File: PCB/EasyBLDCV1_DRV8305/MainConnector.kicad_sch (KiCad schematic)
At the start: 20 parts, among them J1 10159560-A00221RLF, U4 LMR16006XDDCR

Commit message: Colored main connector
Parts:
- L1: footprint EasyBLDC:SD53 -> Inductor_SMD:L_Changjiang_FNR4020S
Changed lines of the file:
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@@
 			)
 		)
-		(property "Footprint" "EasyBLDC:SD53"
+		(property "Footprint" "Inductor_SMD:L_Changjiang_FNR4020S"
 			(at 204.47 45.72 0)
 			(effects

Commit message: Fixed errors with silkscreen overlaping vias. Generated final gerbers.
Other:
- company: Buckley Boards  -> Peter Buckley Engineering
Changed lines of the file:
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@@
 		(date "2024-08-06")
 		(rev "1.0")
-		(company "Buckley Boards ")
+		(company "Peter Buckley Engineering")
 	)
 	(junction

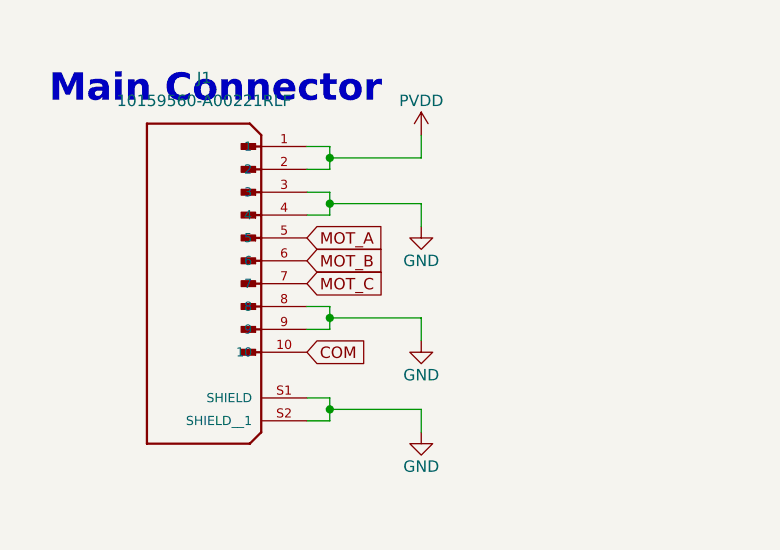
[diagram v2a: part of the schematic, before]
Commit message: Changed main connector pinout to improve signal integrity
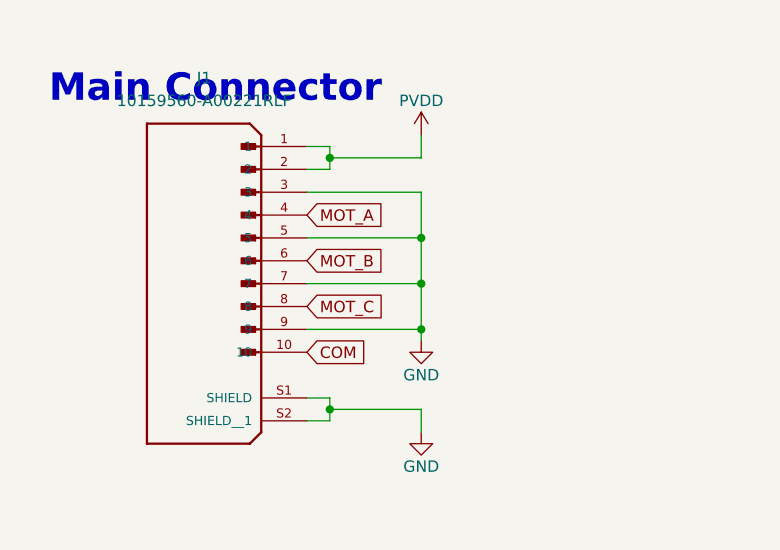
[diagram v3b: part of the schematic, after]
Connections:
- net GND: now also J1.5, J1.7; no longer J1.4, J1.8
- net MOT_A: now also J1.4; no longer J1.5
- net MOT_C: now also J1.8; no longer J1.7
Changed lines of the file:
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@@
-	)
-	(junction
-		(at 78.74 67.31)
-		(diameter 0)
-		(color 0 0 0 0)
 	)
 	(junction
@@
 	)
 	(junction
+		(at 88.9 58.42)
+		(diameter 0)
+		(color 0 0 0 0)
+	)
+	(junction
+		(at 88.9 68.58)
+		(diameter 0)
+		(color 0 0 0 0)
+	)
+	(junction
 		(at 195.58 45.72)
+		(diameter 0)
+		(color 0 0 0 0)
+	)
+	(junction
+		(at 88.9 63.5)
 		(diameter 0)
 		(color 0 0 0 0)
@@
 	)
 	(junction
-		(at 78.74 54.61)
-		(diameter 0)
-		(color 0 0 0 0)
-	)
-	(junction
 		(at 73.66 116.84)
 		(diameter 0)
@@
 	(wire
 		(pts
-			(xy 78.74 68.58) (xy 76.2 68.58)
+			(xy 76.2 68.58) (xy 88.9 68.58)
 		)
 		(stroke
@@
 	(wire
 		(pts
-			(xy 78.74 54.61) (xy 88.9 54.61)
-		)
-		(stroke
-			(width 0)
-			(type default)
-		)
-	)
-	(wire
-		(pts
 			(xy 210.82 76.2) (xy 210.82 78.74)
 		)
@@
 	(wire
 		(pts
+			(xy 88.9 58.42) (xy 88.9 63.5)
+		)
+		(stroke
+			(width 0)
+			(type default)
+		)
+	)
+	(wire
+		(pts
+			(xy 76.2 58.42) (xy 88.9 58.42)
+		)
+		(stroke
+			(width 0)
+			(type default)
+		)
+	)
+	(wire
+		(pts
 			(xy 49.53 114.3) (xy 49.53 116.84)
 		)
@@
 	(wire
 		(pts
-			(xy 76.2 55.88) (xy 78.74 55.88)
-		)
-		(stroke
-			(width 0)
-			(type default)
-		)
-	)
-	(wire
-		(pts
 			(xy 201.93 60.96) (xy 201.93 64.77)
 		)
@@
 	(wire
 		(pts
-			(xy 76.2 66.04) (xy 78.74 66.04)
-		)
-		(stroke
-			(width 0)
-			(type default)
-		)
-	)
-	(wire
-		(pts
 			(xy 182.88 78.74) (xy 210.82 78.74)
 		)
@@
 	(wire
 		(pts
-			(xy 78.74 54.61) (xy 78.74 53.34)
-		)
-		(stroke
-			(width 0)
-			(type default)
-		)
-	)
-	(wire
-		(pts
 			(xy 86.36 135.89) (xy 86.36 137.16)
 		)
@@
 	(wire
 		(pts
-			(xy 78.74 67.31) (xy 88.9 67.31)
-		)
-		(stroke
-			(width 0)
-			(type default)
-		)
-	)
-	(wire
-		(pts
-			(xy 78.74 53.34) (xy 76.2 53.34)
+			(xy 88.9 63.5) (xy 88.9 68.58)
+		)
+		(stroke
+			(width 0)
+			(type default)
+		)
+	)
+	(wire
+		(pts
+			(xy 88.9 53.34) (xy 88.9 58.42)
 		)
 		(stroke
@@
 	(wire
 		(pts
-			(xy 78.74 55.88) (xy 78.74 54.61)
-		)
-		(stroke
-			(width 0)
-			(type default)
-		)
-	)
-	(wire
-		(pts
-			(xy 78.74 66.04) (xy 78.74 67.31)
-		)
-		(stroke
-			(width 0)
-			(type default)
-		)
-	)
-	(wire
-		(pts
 			(xy 78.74 49.53) (xy 88.9 49.53)
 		)
@@
 	(wire
 		(pts
-			(xy 88.9 67.31) (xy 88.9 69.85)
+			(xy 88.9 68.58) (xy 88.9 69.85)
+		)
+		(stroke
+			(width 0)
+			(type default)
+		)
+	)
+	(wire
+		(pts
+			(xy 76.2 63.5) (xy 88.9 63.5)
 		)
 		(stroke
@@
 	(wire
 		(pts
-			(xy 88.9 54.61) (xy 88.9 57.15)
-		)
-		(stroke
-			(width 0)
-			(type default)
-		)
-	)
-	(wire
-		(pts
 			(xy 73.66 125.73) (xy 73.66 127)
 		)
@@
 	(wire
 		(pts
+			(xy 76.2 53.34) (xy 88.9 53.34)
+		)
+		(stroke
+			(width 0)
+			(type default)
+		)
+	)
+	(wire
+		(pts
 			(xy 78.74 48.26) (xy 76.2 48.26)
 		)
@@
 		(pts
 			(xy 59.69 116.84) (xy 59.69 123.19)
-		)
-		(stroke
-			(width 0)
-			(type default)
-		)
-	)
-	(wire
-		(pts
-			(xy 78.74 67.31) (xy 78.74 68.58)
 		)
 		(stroke
@@
 	(global_label "MOT_A"
 		(shape input)
-		(at 76.2 58.42 0)
+		(at 76.2 55.88 0)
 		(fields_autoplaced yes)
 		(effects
@@
 		)
 		(property "Intersheetrefs" "${INTERSHEET_REFS}"
-			(at 84.9909 58.42 0)
+			(at 84.9909 55.88 0)
 			(effects
 				(font
@@
 	(global_label "MOT_C"
 		(shape input)
-		(at 76.2 63.5 0)
+		(at 76.2 66.04 0)
 		(fields_autoplaced yes)
 		(effects
@@
 		)
 		(property "Intersheetrefs" "${INTERSHEET_REFS}"
-			(at 85.1723 63.5 0)
+			(at 85.1723 66.04 0)
 			(effects
 				(font
@@
 					(unit 1)
 				)
-			)
-		)
-	)
-	(symbol
-		(lib_id "power:GND")
-		(at 88.9 57.15 0)
-		(unit 1)
-		(exclude_from_sim no)
-		(in_bom yes)
-		(on_board yes)
-		(dnp no)
-		(property "Reference" "#PWR044"
-			(at 88.9 63.5 0)
-			(effects
-				(font
-					(size 1.27 1.27)
-				)
-				(hide yes)
-			)
-		)
-		(property "Value" "GND"
-			(at 88.9 60.96 0)
-			(effects
-				(font
-					(size 1.27 1.27)
-				)
-			)
-		)
-		(property "Footprint" ""
-			(at 88.9 57.15 0)
-			(effects
-				(font
-					(size 1.27 1.27)
-				)
-				(hide yes)
-			)
-		)
-		(property "Datasheet" ""
-			(at 88.9 57.15 0)
-			(effects
-				(font
-					(size 1.27 1.27)
-				)
-				(hide yes)
-			)
-		)
-		(property "Description" "Power symbol creates a global label with name \"GND\" , ground"
-			(at 88.9 57.15 0)
-			(effects
-				(font
-					(size 1.27 1.27)
-				)
-				(hide yes)
-			)
-		)
-		(pin "1"
-		)
-		(instances
-			(project "EasyESCV1_DRV8305"
-				(path "/6c304649-7c80-4a4c-b925-07b9210ad53d/22fb4715-9f33-45f1-b8d4-9537d945fe69"
-					(reference "#PWR044")
-					(unit 1)
-				)

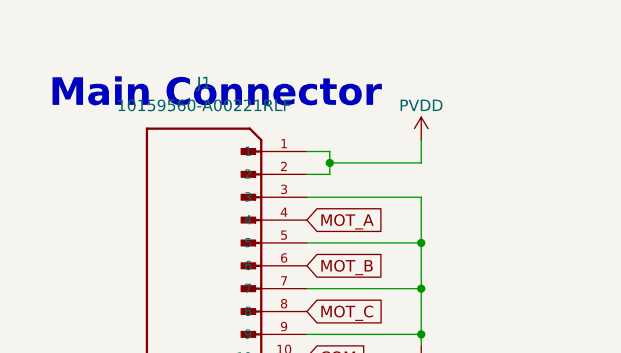
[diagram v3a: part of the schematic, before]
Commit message: JTAG Connector Changed
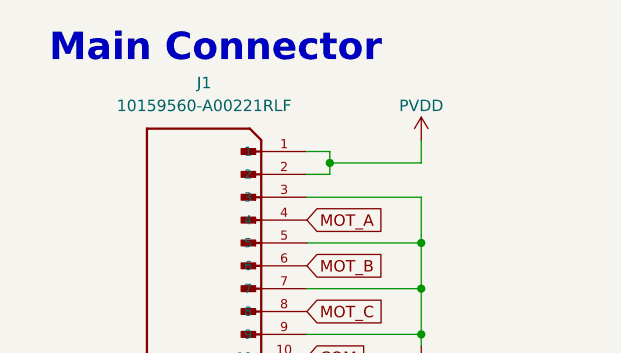
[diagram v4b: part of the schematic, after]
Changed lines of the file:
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@@
 	(text "Main Connector"
 		(exclude_from_sim no)
-		(at 66.04 41.91 0)
+		(at 66.04 36.83 0)
 		(effects
 			(font
